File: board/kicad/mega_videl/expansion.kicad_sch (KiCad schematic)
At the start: 5 parts, among them J1 Conn_02x07_Odd_Even, J5 Conn_02x25_Odd_Even, J6 Conn_02x25_Odd_Even, U6 74LVC245ABQ

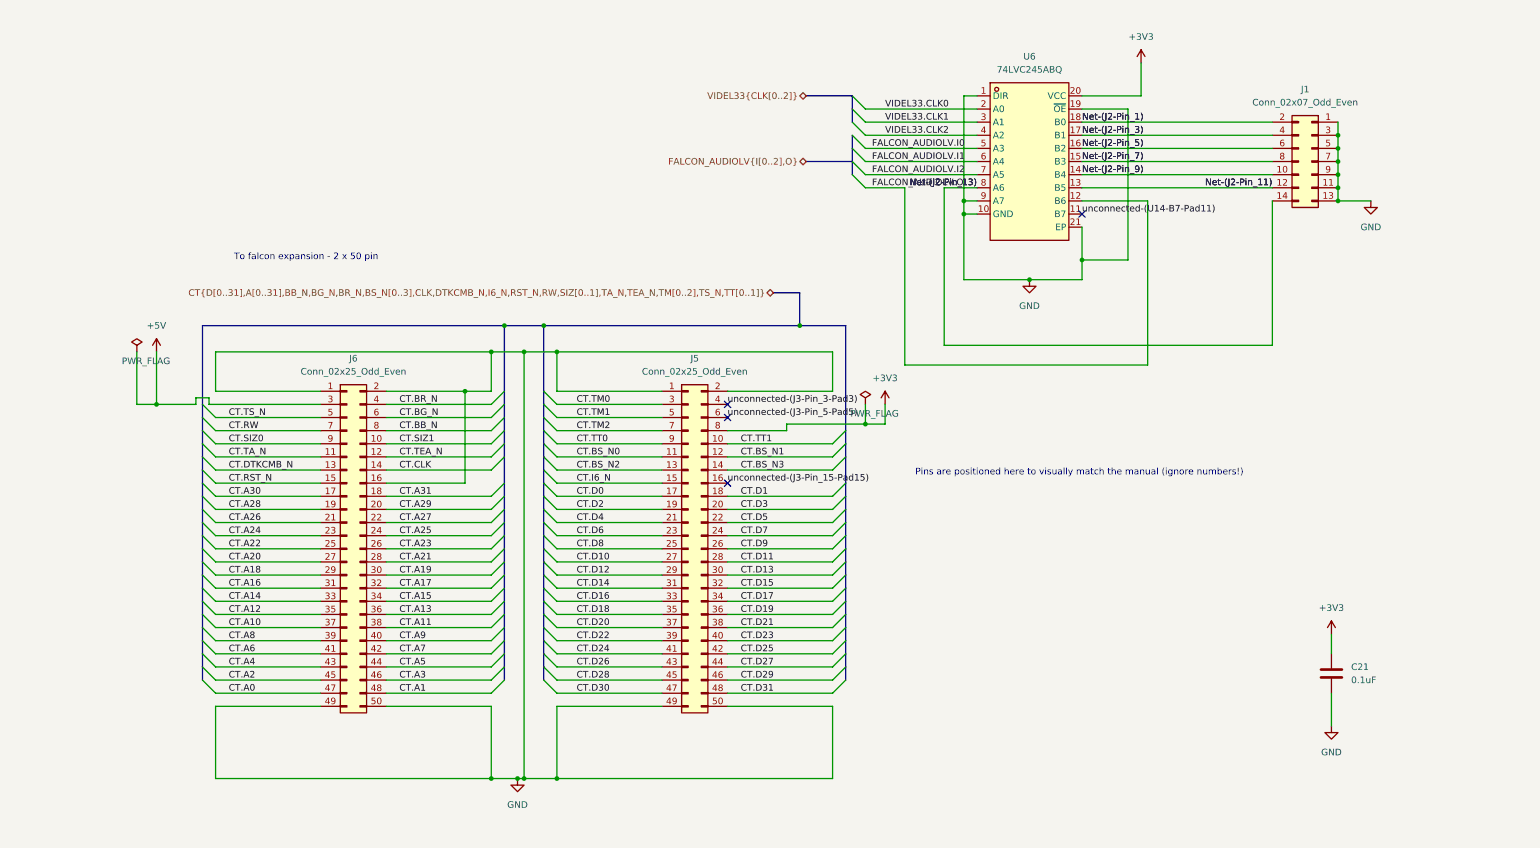
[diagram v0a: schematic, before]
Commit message: Reviewed and fixed many issues. e.g. missing decoupling for 1.35v under fpga
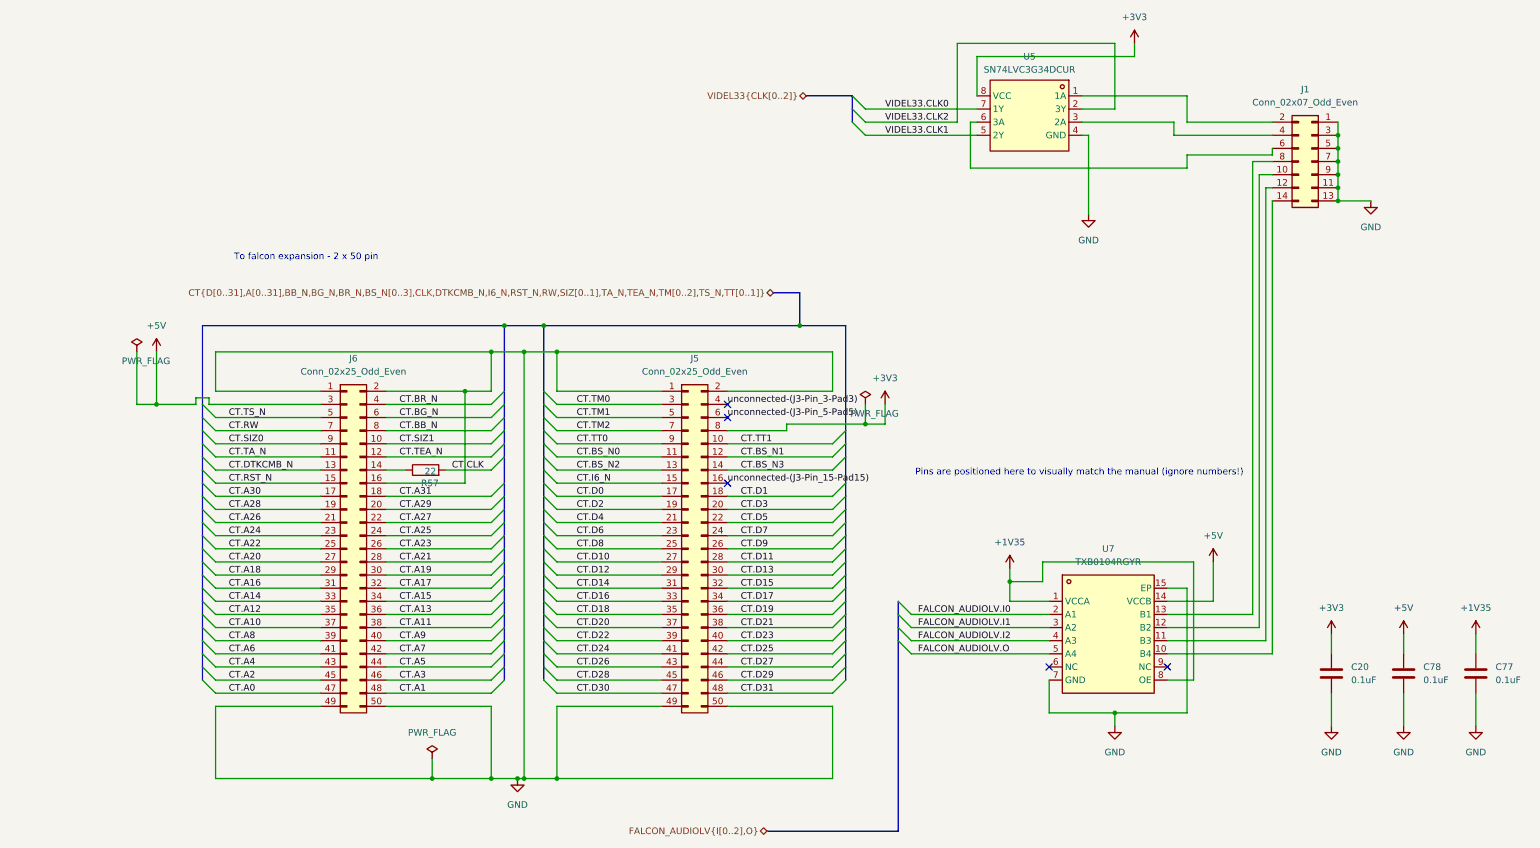
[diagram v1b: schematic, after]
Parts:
- removed U6: 74LVC245ABQ, mega_videl:DHVQFN20_L4.5-W2.5-P0.50-BL, symbol mega_videl:74LVC245ABQ
- added C77, C78: 0.1uF, Capacitor_SMD:C_0603_1608Metric, symbol Device:C
- added R57: 22, Resistor_SMD:R_0603_1608Metric, symbol Device:R
- added U5: SN74LVC3G34DCUR, mega_videl:VSSOP-8_L2.1-W2.4-P0.50-LS3.2-BR, symbol mega_videl:SN74LVC3G34DCUR
- added U7: TXB0104RGYR, mega_videl:VQFN-14_L3.5-W3.5-P0.50-BL-EP, symbol mega_videl:TXB0104RGYR
- J5, J6: KiLib_Generator (none) -> connector/pin_header_socket
- renumbered C21 to C20
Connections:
- net +3V3: now also U5.8 (VCC)
- net +5V: now also C78.1, U7.14 (VCCB)
- net CT.CLK: now also R57.2; no longer J6.14 (Pin_14)
- net FALCON_AUDIOLV.I0: now also U7.2 (A1)
- net FALCON_AUDIOLV.I1: now also U7.3 (A2)
- net FALCON_AUDIOLV.I2: now also U7.4 (A3)
- net FALCON_AUDIOLV.O: now also U7.5 (A4)
- net GND: now also C77.2, C78.2, U5.4 (GND), U7.15 (EP), U7.7 (GND)
- net VIDEL33.CLK0: now also U5.7 (1Y)
- net VIDEL33.CLK1: now also U5.5 (2Y)
- net VIDEL33.CLK2: now also U5.2 (3Y)
- net Net-(J2-Pin_1): no longer names the net of J1.2 (Pin_2)
- net Net-(J2-Pin_1): now also U5.1 (1A)
- net Net-(J2-Pin_11): no longer names the net of J1.12 (Pin_12)
- net Net-(J2-Pin_11): now also U7.11 (B3)
- net Net-(J2-Pin_13): no longer names the net of J1.14 (Pin_14)
- net Net-(J2-Pin_13): now also U7.10 (B4)
- net Net-(J2-Pin_3): no longer names the net of J1.4 (Pin_4)
- net Net-(J2-Pin_3): now also U5.3 (2A)
- net Net-(J2-Pin_5): no longer names the net of J1.6 (Pin_6)
- net Net-(J2-Pin_5): now also U5.6 (3A)
- net Net-(J2-Pin_7): no longer names the net of J1.8 (Pin_8)
- net Net-(J2-Pin_7): now also U7.13 (B1)
- net Net-(J2-Pin_9): no longer names the net of J1.10 (Pin_10)
- net Net-(J2-Pin_9): now also U7.12 (B2)
- new net: J6.14 (Pin_14), R57.1
- new net +1V35: C77.1, U7.1 (VCCA), U7.8 (OE)
- no-connect marks 4 -> 5

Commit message: Assigned all parts with JLCPCB plugin
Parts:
- C20, C77, C78: LCSC (none) -> C14663
- J1: LCSC (none) -> C3975152
- J5, J6: LCSC (none) -> C52611
- R57: KiLib_Generator (none) -> SMD_2terminal_chip_molded; LCSC (none) -> C23345
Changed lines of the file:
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@@
+			)
+		)
+		(property "LCSC" "C3975152"
+			(at 241.3 39.37 0)
+			(hide yes)
+			(show_name no)
+			(do_not_autoplace no)
+			(effects
+				(font
+					(size 1.27 1.27)
+				)
 			)
 		)
@@
 			)
 		)
+		(property "LCSC" "C14663"
+			(at 259.08 138.43 0)
+			(hide yes)
+			(show_name no)
+			(do_not_autoplace no)
+			(effects
+				(font
+					(size 1.27 1.27)
+				)
+			)
+		)
 		(pin "1"
 		)
@@
 			)
 		)
+		(property "KiLib_Generator" "SMD_2terminal_chip_molded"
+			(at 69.85 99.06 0)
+			(hide yes)
+			(show_name no)
+			(do_not_autoplace no)
+			(effects
+				(font
+					(size 1.27 1.27)
+				)
+			)
+		)
+		(property "LCSC" "C23345"
+			(at 69.85 99.06 0)
+			(hide yes)
+			(show_name no)
+			(do_not_autoplace no)
+			(effects
+				(font
+					(size 1.27 1.27)
+				)
+			)
+		)
 		(pin "2"
 		)
@@
 			)
 		)
+		(property "LCSC" "C14663"
+			(at 245.11 138.43 0)
+			(hide yes)
+			(show_name no)
+			(do_not_autoplace no)
+			(effects
+				(font
+					(size 1.27 1.27)
+				)
+			)
+		)
 		(pin "1"
 		)
@@
 			)
 		)
+		(property "LCSC" "C52611"
+			(at 120.65 114.3 0)
+			(hide yes)
+			(show_name no)
+			(do_not_autoplace no)
+			(effects
+				(font
+					(size 1.27 1.27)
+				)
+			)
+		)
 		(pin "7"
 		)
@@
 			)
 		)
+		(property "LCSC" "C14663"
+			(at 273.05 138.43 0)
+			(hide yes)
+			(show_name no)
+			(do_not_autoplace no)
+			(effects
+				(font
+					(size 1.27 1.27)
+				)
+			)
+		)
 		(pin "1"
 		)
@@
 			(at 54.61 114.3 0)
 			(hide yes)
+			(show_name no)
+			(do_not_autoplace no)
+			(effects
+				(font
+					(size 1.27 1.27)
+				)
+			)
+		)
+		(property "LCSC" "C52611"
+			(at 54.61 114.3 0)
+			(hide yes)

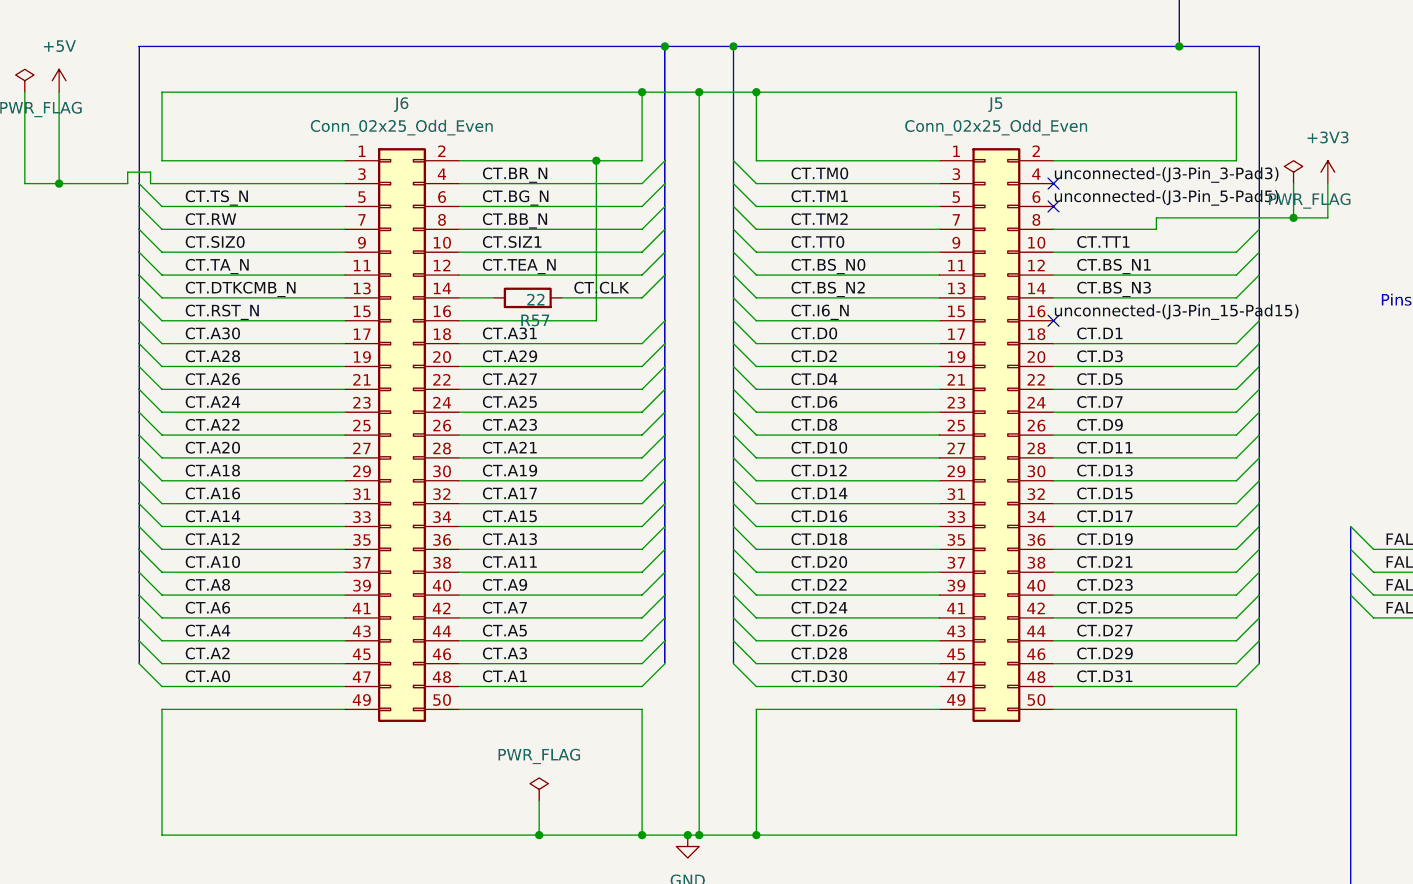
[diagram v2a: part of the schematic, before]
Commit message: Added series resistors to all CT lines. They ring up to 7V apparently according to Super Videl devs. Some of that is likely the length of scope lines. The safety fix here is to add small 33ohm resistors and to enable clamp diodes in the FPGA core.
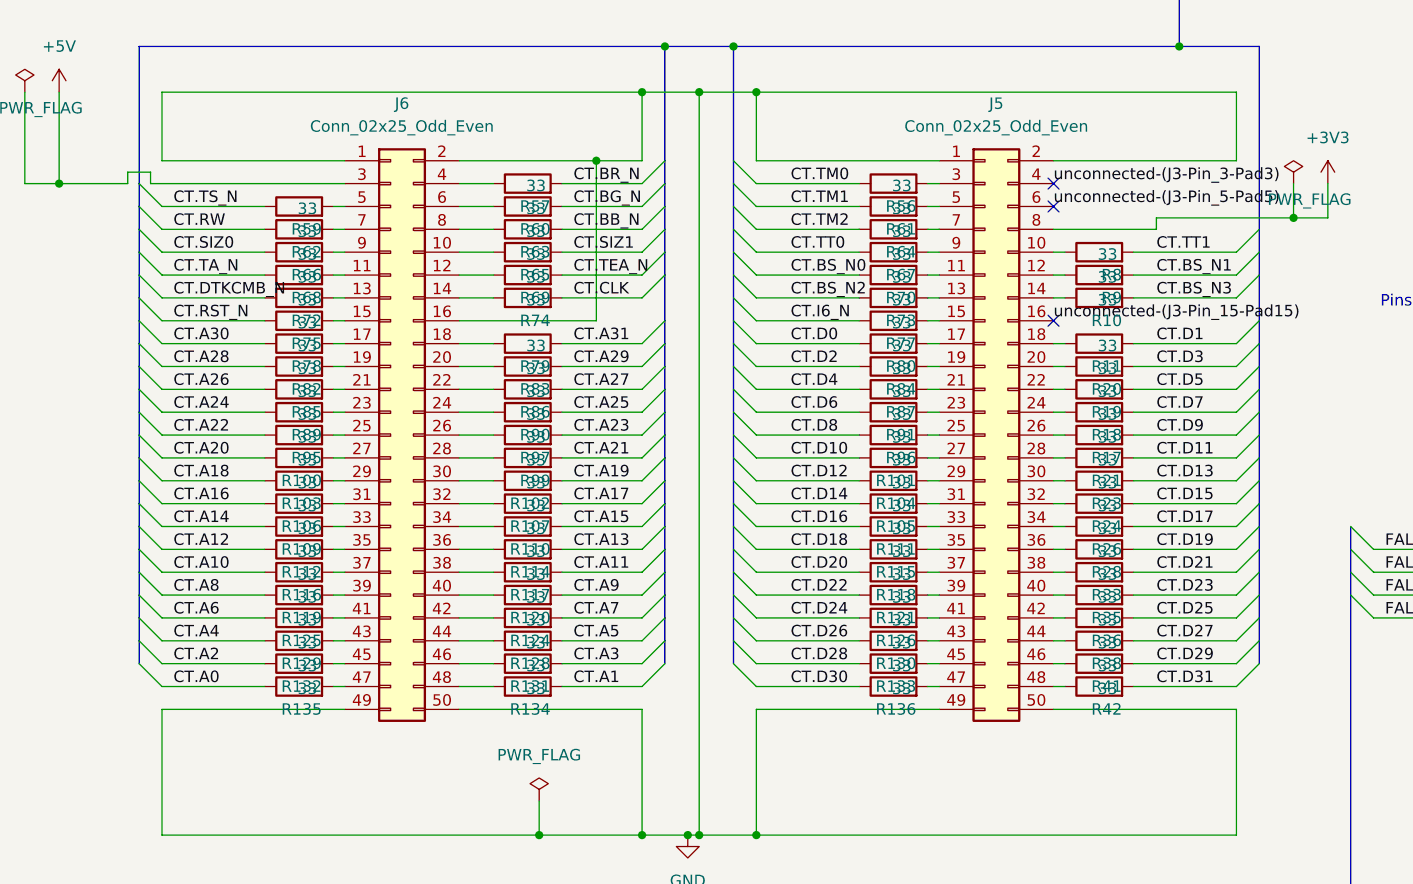
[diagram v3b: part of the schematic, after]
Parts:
- added R10, R100, R101, R102, R103, R104, R105, R106, R107, R109, R11, R110, R111, R112, R114, R115, R116, R117, R118, R119, R120, R121, R124, R125, R126, R128, R129, R130, R131, R132, R133, R134, R135, R136, R17, R18, R19, R20, R21, R23, R24, R26, R28, R33, R35, R36, R38, R41, R42, R56, R57, R59, R60, R61, R62, R63, R64, R65, R66, R67, R68, R69, R70, R72, R73, R75, R77, R78, R79, R8, R80, R82, R83, R84, R85, R86, R87, R89, R9, R90, R91, R95, R96, R97, R99: 33, Resistor_SMD:R_0402_1005Metric, symbol Device:R
- R74: renamed from R57; value 22 -> 33; footprint Resistor_SMD:R_0603_1608Metric -> Resistor_SMD:R_0402_1005Metric; LCSC C23345 -> C25105
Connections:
- net CT.A0: now also R135.1; no longer J6.47 (Pin_47)
- net CT.A1: now also R134.2; no longer J6.48 (Pin_48)
- net CT.A10: now also R116.1; no longer J6.37 (Pin_37)
- net CT.A11: now also R117.2; no longer J6.38 (Pin_38)
- net CT.A12: now also R112.1; no longer J6.35 (Pin_35)
- net CT.A13: now also R114.2; no longer J6.36 (Pin_36)
- net CT.A14: now also R109.1; no longer J6.33 (Pin_33)
- net CT.A15: now also R110.2; no longer J6.34 (Pin_34)
- net CT.A16: now also R106.1; no longer J6.31 (Pin_31)
- net CT.A17: now also R107.2; no longer J6.32 (Pin_32)
- net CT.A18: now also R103.1; no longer J6.29 (Pin_29)
- net CT.A19: now also R102.2; no longer J6.30 (Pin_30)
- net CT.A2: now also R132.1; no longer J6.45 (Pin_45)
- net CT.A20: now also R100.1; no longer J6.27 (Pin_27)
- net CT.A21: now also R99.2; no longer J6.28 (Pin_28)
- net CT.A22: now also R95.1; no longer J6.25 (Pin_25)
- net CT.A23: now also R97.2; no longer J6.26 (Pin_26)
- net CT.A24: now also R89.1; no longer J6.23 (Pin_23)
- net CT.A25: now also R90.2; no longer J6.24 (Pin_24)
- net CT.A26: now also R85.1; no longer J6.21 (Pin_21)
- net CT.A27: now also R86.2; no longer J6.22 (Pin_22)
- net CT.A28: now also R82.1; no longer J6.19 (Pin_19)
- net CT.A29: now also R83.2; no longer J6.20 (Pin_20)
- net CT.A3: now also R131.2; no longer J6.46 (Pin_46)
- net CT.A30: now also R78.1; no longer J6.17 (Pin_17)
- net CT.A31: now also R79.2; no longer J6.18 (Pin_18)
- net CT.A4: now also R129.1; no longer J6.43 (Pin_43)
- net CT.A5: now also R128.2; no longer J6.44 (Pin_44)
- net CT.A6: now also R125.1; no longer J6.41 (Pin_41)
- net CT.A7: now also R124.2; no longer J6.42 (Pin_42)
- net CT.A8: now also R119.1; no longer J6.39 (Pin_39)
- net CT.A9: now also R120.2; no longer J6.40 (Pin_40)
- net CT.BB_N: now also R63.2; no longer J6.8 (Pin_8)
- net CT.BG_N: now also R60.2; no longer J6.6 (Pin_6)
- net CT.BR_N: now also R57.2; no longer J6.4 (Pin_4)
- net CT.BS_N0: now also R70.1; no longer J5.11 (Pin_11)
- net CT.BS_N1: now also R9.2; no longer J5.12 (Pin_12)
- net CT.BS_N2: now also R73.1; no longer J5.13 (Pin_13)
- net CT.BS_N3: now also R10.2; no longer J5.14 (Pin_14)
- net CT.D0: now also R80.1; no longer J5.17 (Pin_17)
- net CT.D1: now also R11.2; no longer J5.18 (Pin_18)
- net CT.D10: now also R101.1; no longer J5.27 (Pin_27)
- net CT.D11: now also R21.2; no longer J5.28 (Pin_28)
- net CT.D12: now also R104.1; no longer J5.29 (Pin_29)
- net CT.D13: now also R23.2; no longer J5.30 (Pin_30)
- net CT.D14: now also R105.1; no longer J5.31 (Pin_31)
- net CT.D15: now also R24.2; no longer J5.32 (Pin_32)
- net CT.D16: now also R111.1; no longer J5.33 (Pin_33)
- net CT.D17: now also R26.2; no longer J5.34 (Pin_34)
- net CT.D18: now also R115.1; no longer J5.35 (Pin_35)
- net CT.D19: now also R28.2; no longer J5.36 (Pin_36)
- net CT.D2: now also R84.1; no longer J5.19 (Pin_19)
- net CT.D20: now also R118.1; no longer J5.37 (Pin_37)
- net CT.D21: now also R33.2; no longer J5.38 (Pin_38)
- net CT.D22: now also R121.1; no longer J5.39 (Pin_39)
- net CT.D23: now also R35.2; no longer J5.40 (Pin_40)
- net CT.D24: now also R126.1; no longer J5.41 (Pin_41)
- net CT.D25: now also R36.2; no longer J5.42 (Pin_42)
- net CT.D26: now also R130.1; no longer J5.43 (Pin_43)
- net CT.D27: now also R38.2; no longer J5.44 (Pin_44)
- net CT.D28: now also R133.1; no longer J5.45 (Pin_45)
- net CT.D29: now also R41.2; no longer J5.46 (Pin_46)
- net CT.D3: now also R20.2; no longer J5.20 (Pin_20)
- net CT.D30: now also R136.1; no longer J5.47 (Pin_47)
- net CT.D31: now also R42.2; no longer J5.48 (Pin_48)
- net CT.D4: now also R87.1; no longer J5.21 (Pin_21)
- net CT.D5: now also R19.2; no longer J5.22 (Pin_22)
- net CT.D6: now also R91.1; no longer J5.23 (Pin_23)
- net CT.D7: now also R18.2; no longer J5.24 (Pin_24)
- net CT.D8: now also R96.1; no longer J5.25 (Pin_25)
- net CT.D9: now also R17.2; no longer J5.26 (Pin_26)
- net CT.DTKCMB_N: now also R72.1; no longer J6.13 (Pin_13)
- net CT.I6_N: now also R77.1; no longer J5.15 (Pin_15)
- net CT.RST_N: now also R75.1; no longer J6.15 (Pin_15)
- net CT.RW: now also R62.1; no longer J6.7 (Pin_7)
- net CT.SIZ0: now also R66.1; no longer J6.9 (Pin_9)
- net CT.SIZ1: now also R65.2; no longer J6.10 (Pin_10)
- net CT.TA_N: now also R68.1; no longer J6.11 (Pin_11)
- net CT.TEA_N: now also R69.2; no longer J6.12 (Pin_12)
- net CT.TM0: now also R56.1; no longer J5.3 (Pin_3)
- net CT.TM1: now also R61.1; no longer J5.5 (Pin_5)
- net CT.TM2: now also R64.1; no longer J5.7 (Pin_7)
- net CT.TS_N: now also R59.1; no longer J6.5 (Pin_5)
- net CT.TT0: now also R67.1; no longer J5.9 (Pin_9)
- net CT.TT1: now also R8.2; no longer J5.10 (Pin_10)
- new net: J5.42 (Pin_42), R36.1
- new net: J5.5 (Pin_5), R61.2
- new net: J6.41 (Pin_41), R125.2
- new net: J6.45 (Pin_45), R132.2
- new net: J6.17 (Pin_17), R78.2
- new net: J5.18 (Pin_18), R11.1
- new net: J5.23 (Pin_23), R91.2
- new net: J6.30 (Pin_30), R102.1
- new net: J5.21 (Pin_21), R87.2
- new net: J5.40 (Pin_40), R35.1
- new net: J5.27 (Pin_27), R101.2
- new net: J6.6 (Pin_6), R60.1
- new net: J5.19 (Pin_19), R84.2
- new net: J5.48 (Pin_48), R42.1
- new net: J6.37 (Pin_37), R116.2
- new net: J5.29 (Pin_29), R104.2
- new net: J6.19 (Pin_19), R82.2
- new net: J6.32 (Pin_32), R107.1
- new net: J5.15 (Pin_15), R77.2
- new net: J5.45 (Pin_45), R133.2
- new net: J6.28 (Pin_28), R99.1
- new net: J6.21 (Pin_21), R85.2
- new net: J6.24 (Pin_24), R90.1
- new net: J5.14 (Pin_14), R10.1
- new net: J5.12 (Pin_12), R9.1
- new net: J6.34 (Pin_34), R110.1
- new net: J5.39 (Pin_39), R121.2
- new net: J5.9 (Pin_9), R67.2
- new net: J6.39 (Pin_39), R119.2
- new net: J6.38 (Pin_38), R117.1
- new net: J5.7 (Pin_7), R64.2
- new net: J5.31 (Pin_31), R105.2
- new net: J5.30 (Pin_30), R23.1
- new net: J6.12 (Pin_12), R69.1
- new net: J6.7 (Pin_7), R62.2
- new net: J5.47 (Pin_47), R136.2
- new net: J5.43 (Pin_43), R130.2
- new net: J5.32 (Pin_32), R24.1
- new net: J5.46 (Pin_46), R41.1
- new net: J6.43 (Pin_43), R129.2
- new net: J6.36 (Pin_36), R114.1
- new net: J6.18 (Pin_18), R79.1
- new net: J6.33 (Pin_33), R109.2
- new net: J6.15 (Pin_15), R75.2
- new net: J6.20 (Pin_20), R83.1
- new net: J6.10 (Pin_10), R65.1
- new net: J5.17 (Pin_17), R80.2
- new net: J5.10 (Pin_10), R8.1
- new net: J5.33 (Pin_33), R111.2
- new net: J6.4 (Pin_4), R57.1
- new net: J6.22 (Pin_22), R86.1
- new net: J6.9 (Pin_9), R66.2
- new net: J5.38 (Pin_38), R33.1
- new net: J6.48 (Pin_48), R134.1
- new net: J5.37 (Pin_37), R118.2
- new net: J6.27 (Pin_27), R100.2
- new net: J5.44 (Pin_44), R38.1
- new net: J6.29 (Pin_29), R103.2
- new net: J6.26 (Pin_26), R97.1
- new net: J6.13 (Pin_13), R72.2
- new net: J5.26 (Pin_26), R17.1
- new net: J6.42 (Pin_42), R124.1
- new net: J5.24 (Pin_24), R18.1
- new net: J6.44 (Pin_44), R128.1
- new net: J5.11 (Pin_11), R70.2
- new net: J5.13 (Pin_13), R73.2
- new net: J5.20 (Pin_20), R20.1
- new net: J5.22 (Pin_22), R19.1
- new net: J5.25 (Pin_25), R96.2
- new net: J5.28 (Pin_28), R21.1
- new net: J5.3 (Pin_3), R56.2
- new net: J5.34 (Pin_34), R26.1
- new net: J5.35 (Pin_35), R115.2
- new net: J5.36 (Pin_36), R28.1
- new net: J5.41 (Pin_41), R126.2
- new net: J6.8 (Pin_8), R63.1
- new net: J6.11 (Pin_11), R68.2
- new net: J6.5 (Pin_5), R59.2
- new net: J6.35 (Pin_35), R112.2
- new net: J6.47 (Pin_47), R135.2
- new net: J6.40 (Pin_40), R120.1
- new net: J6.25 (Pin_25), R95.2
- new net: J6.46 (Pin_46), R131.1
- new net: J6.23 (Pin_23), R89.2
- new net: J6.31 (Pin_31), R106.2

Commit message: Shrunk the dimensions to fit better so it does not hit Q1. Added a notch for the DIMM casing.
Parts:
- J1: LCSC C3975152 -> C7366128
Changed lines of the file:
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@@
 			)
 		)
-		(property "LCSC" "C3975152"
+		(property "LCSC" "C7366128"
 			(at 241.3 39.37 0)
 			(hide yes)
